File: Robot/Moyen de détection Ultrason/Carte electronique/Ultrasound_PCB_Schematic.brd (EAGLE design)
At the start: 80 x 80 mm, 28 parts, among them IC1 74HC595N, X1 JST-XH-06-PIN-ROUND-PAD, X2 JST-XH-03-PIN-ROUND-PAD

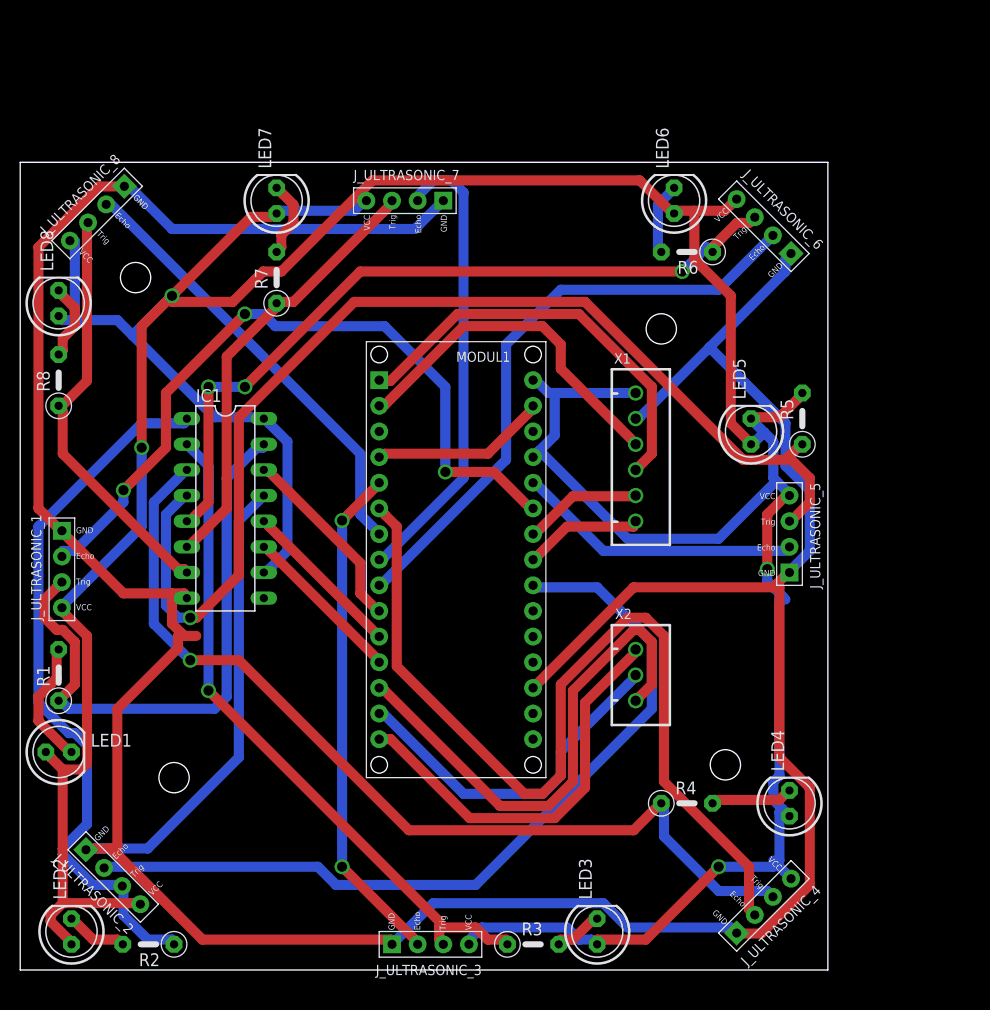
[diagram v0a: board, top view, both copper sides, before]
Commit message: Nouvelle version des fichiers
la nouvelle version est due au fait que l'ancienne était trop grande, eh oui, un carré de 8cm a une diagonale de 11.3 cm (supérieur au 10cm max😭) par conséquent, j'ai créé un nouveau design, qui convient mieux puisqu'il est ajusté avec le modèle de l'impression 3D réalisée auparavant.
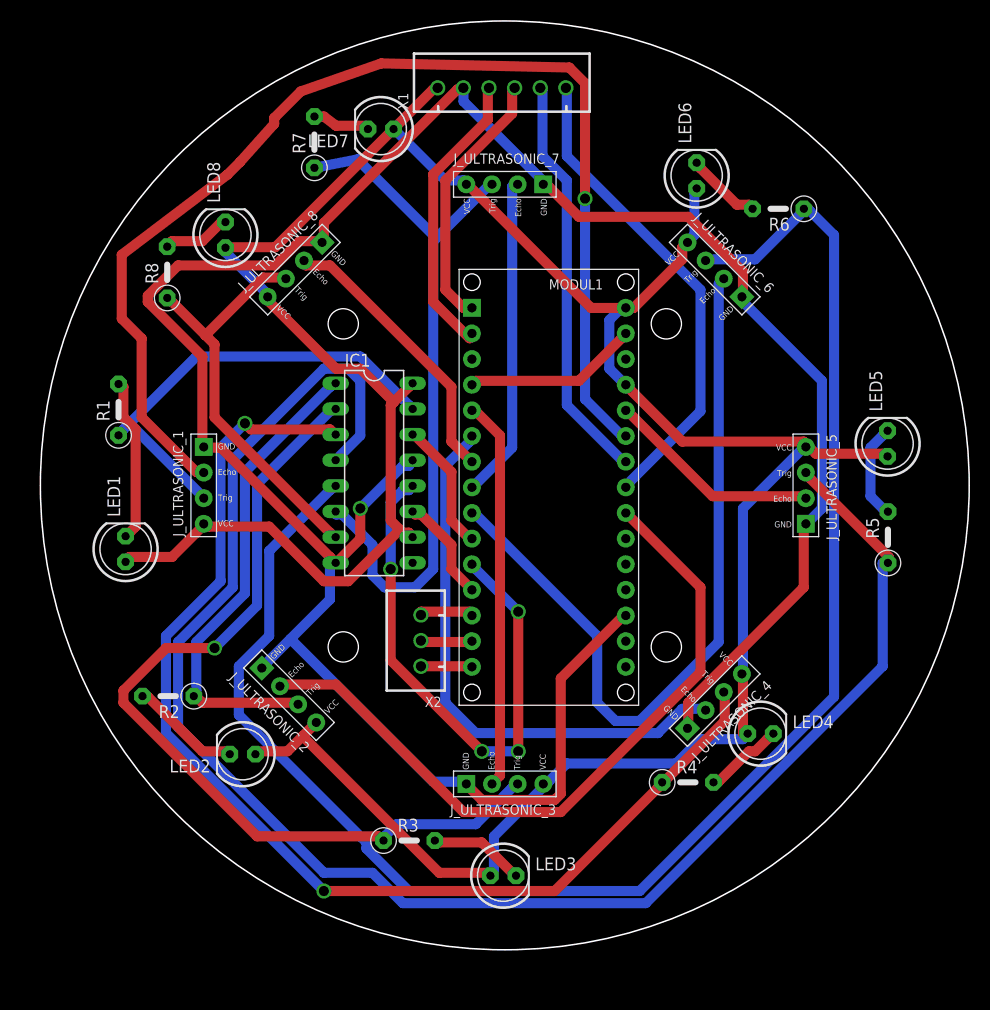
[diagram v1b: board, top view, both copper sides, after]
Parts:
- moved X1 38.9 mm to (47.7, 87.4), turned to 0 degrees
- moved R1 26.9 mm to (9.74, 55.5)
- moved J_ULTRASONIC_2 25.0 mm to (26.6, 27.2)
- moved R2 24.7 mm to (14.7, 27.1)
- moved LED2 24.4 mm to (22.0, 21.4), turned to 180 degrees
- moved X2 21.5 mm to (39.7, 32.6), turned to 90 degrees
- moved LED1 21.2 mm to (10.4, 41.7), turned to 90 degrees
- moved J_ULTRASONIC_4 20.9 mm to (68.8, 26.6)
- moved J_ULTRASONIC_8 20.4 mm to (27.2, 69.4)
- moved LED8 17.9 mm to (20.3, 72.8)
- moved J_ULTRASONIC_3 17.5 mm to (48.0, 18.4)
- moved J_ULTRASONIC_1 16.3 mm to (18.2, 48.0)
- moved R3 16.0 mm to (38.5, 12.8)
- moved R8 15.2 mm to (14.6, 69.1)
- moved IC1 15.1 mm to (35.1, 49.2)
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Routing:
- net GND: track 358.2 -> 247.5 mm, vias 0 -> 1
- net VCC: track 387.4 -> 282.3 mm, vias 4 -> 0
- net N$15: track 76.0 -> 162.9 mm, vias 3 -> 0
- net N$16: track 112.7 -> 164.3 mm, vias 1 -> 0
- net N$29: track 51.3 -> 5.59 mm
- net N$2: track 73.6 -> 115.7 mm, vias 3 -> 1
- net N$18: track 16.2 -> 55.3 mm, vias 0 -> 4
- net N$7: track 92.7 -> 55.5 mm
- net N$26: track 11.9 -> 48.1 mm
- net N$27: track 40.6 -> 5.06 mm
- net N$28: track 35.0 -> 5.19 mm
- net N$25: track 11.7 -> 40.7 mm
- net N$14: track 43.6 -> 71.4 mm
- net N$10: track 71.4 -> 47.5 mm
- net N$12: track 93.1 -> 115.1 mm, vias 1 -> 2
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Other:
- board size 80 x 80 mm -> 92 x 92 mm
